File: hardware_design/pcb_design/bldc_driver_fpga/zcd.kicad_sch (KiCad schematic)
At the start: 8 parts, among them U1 LM339

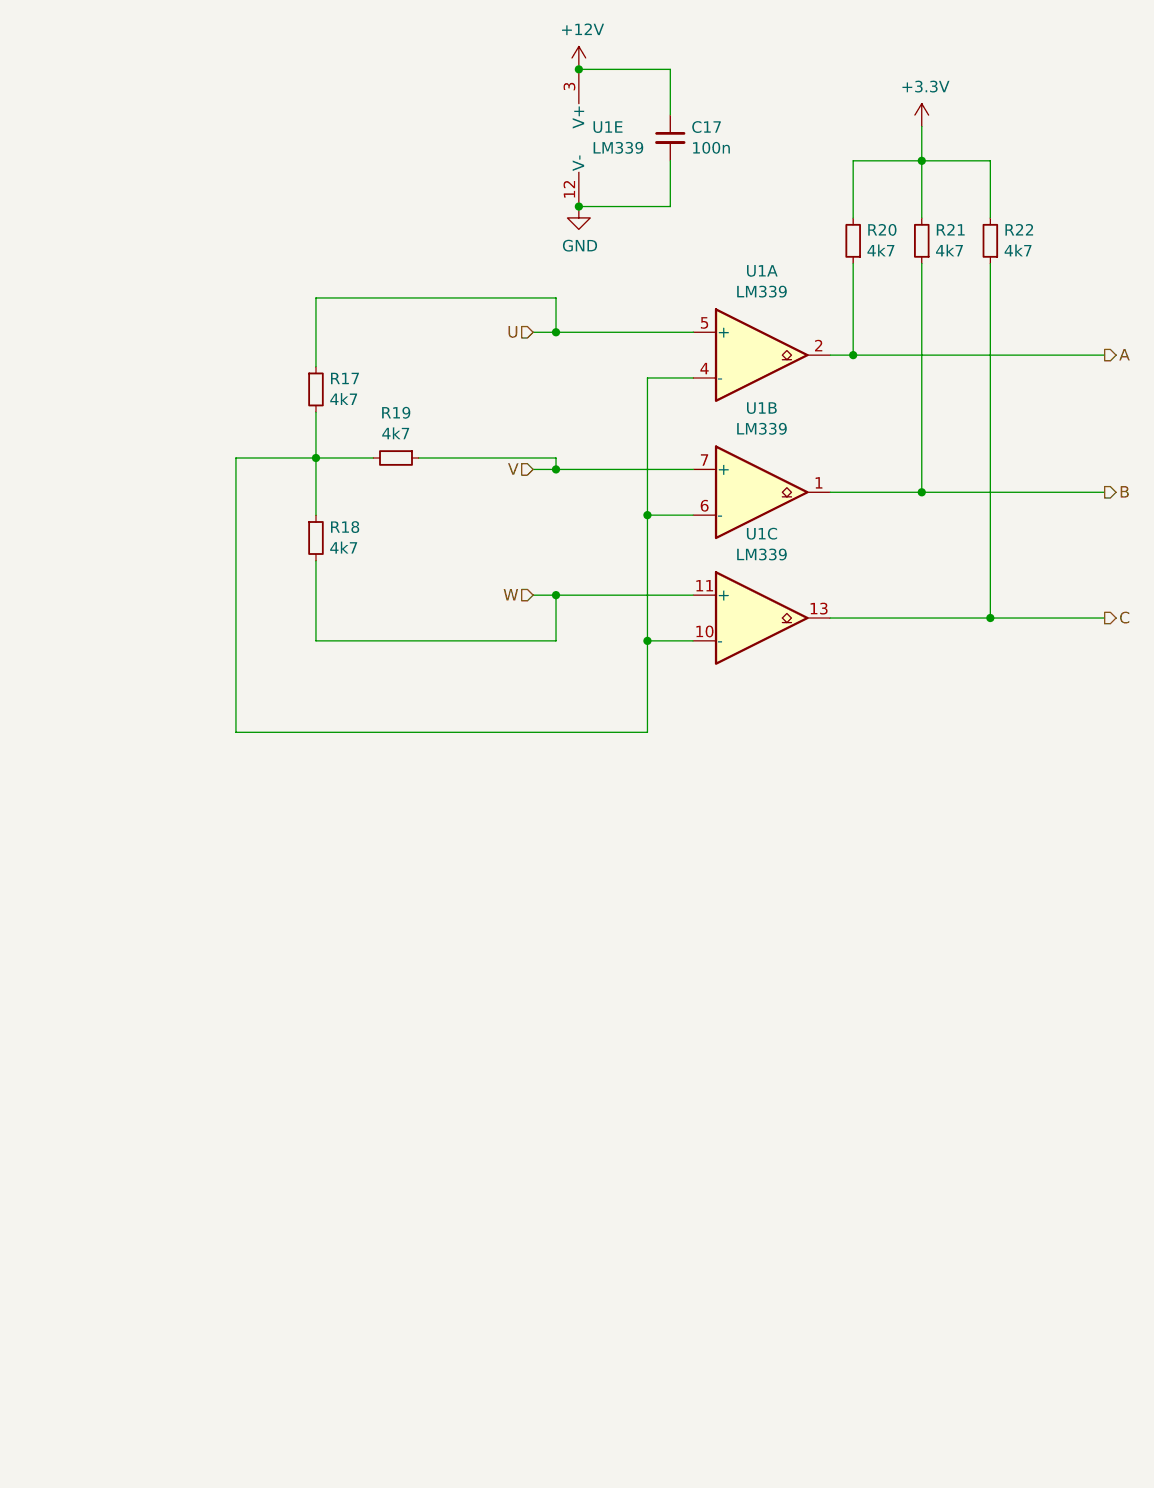
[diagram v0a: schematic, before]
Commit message: Implemented pure sinewave drive from programmable logic. Set up time base generator for ADC.
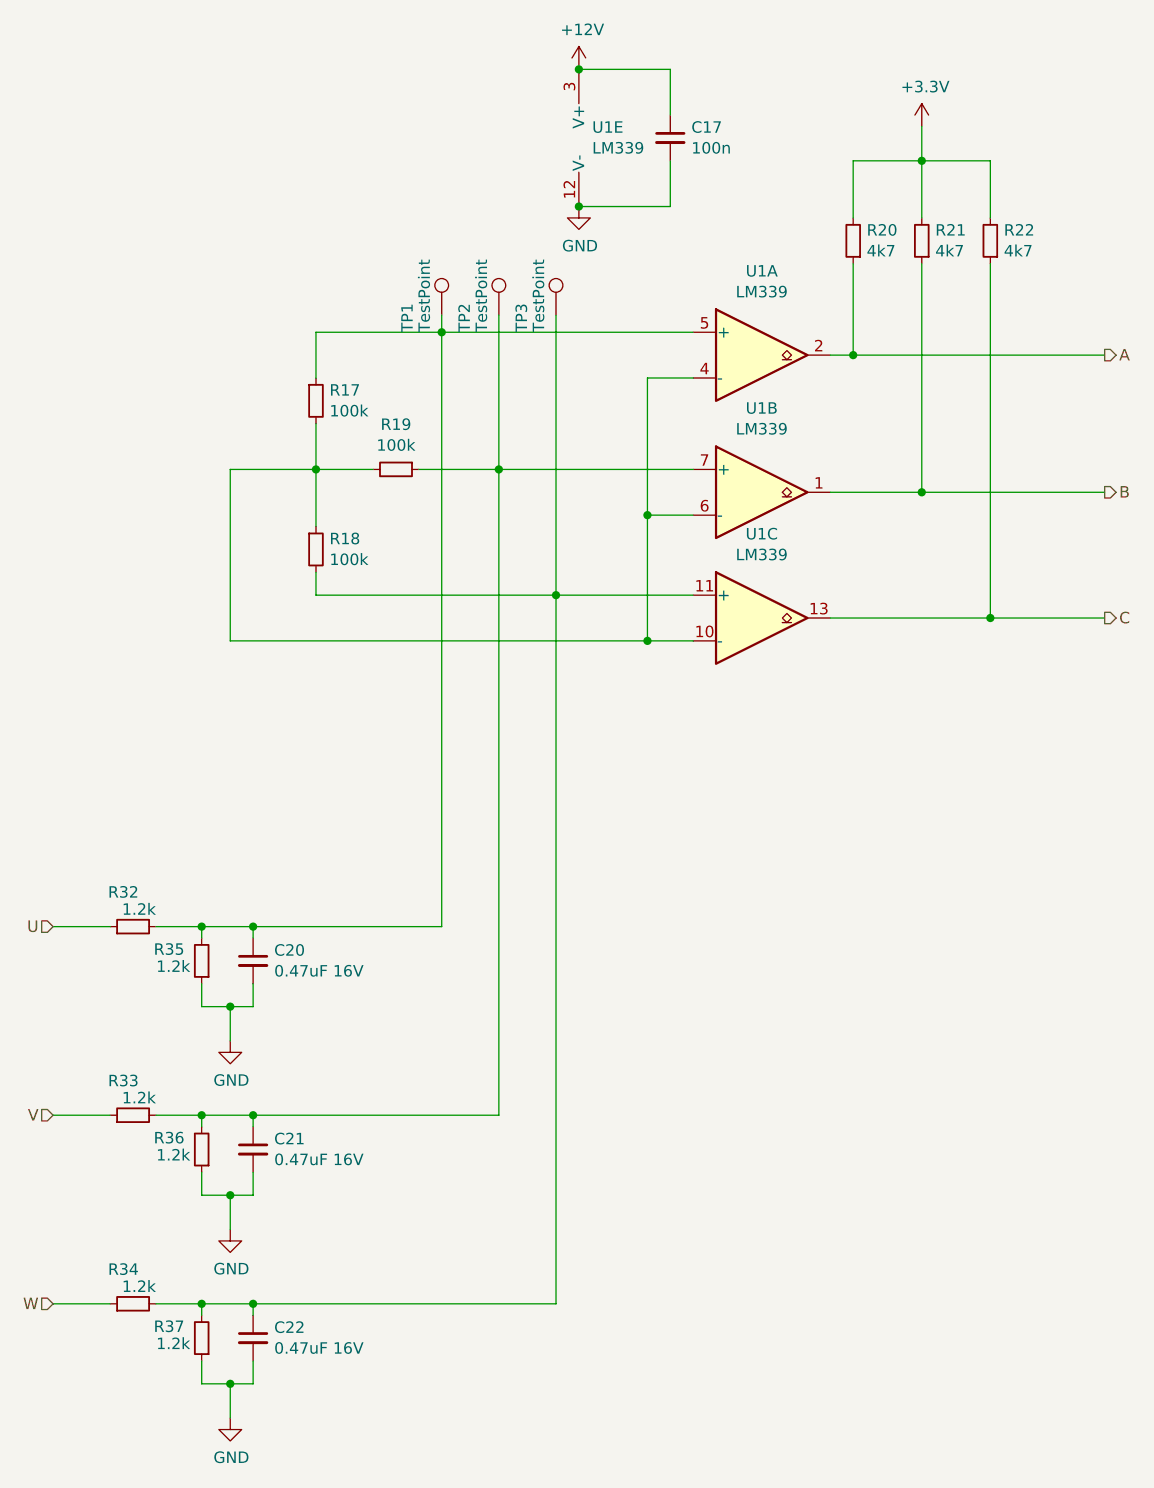
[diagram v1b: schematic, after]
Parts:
- added C20, C21, C22: 0.47uF 16V, Capacitor_SMD:C_0603_1608Metric_Pad1.08x0.95mm_HandSolder, symbol Device:C_Small
- added R32, R33, R34, R35, R36, R37: 1.2k, Resistor_SMD:R_0603_1608Metric_Pad0.98x0.95mm_HandSolder, symbol Device:R_Small
- added TP1, TP2, TP3: TestPoint, TestPoint:TestPoint_Pad_1.0x1.0mm, symbol Connector:TestPoint
- C17: footprint Capacitor_SMD:C_0805_2012Metric_Pad1.15x1.40mm_HandSolder -> Capacitor_SMD:C_0603_1608Metric_Pad1.08x0.95mm_HandSolder
- R17, R18, R19: value 4k7 -> 100k; footprint Resistor_SMD:R_0805_2012Metric_Pad1.15x1.40mm_HandSolder -> Resistor_SMD:R_0603_1608Metric_Pad0.98x0.95mm_HandSolder
- R20, R21, R22: footprint Resistor_SMD:R_0805_2012Metric_Pad1.15x1.40mm_HandSolder -> Resistor_SMD:R_0603_1608Metric_Pad0.98x0.95mm_HandSolder
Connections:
- net GND: now also C20.2, C21.2, C22.2, R35.1, R36.1, R37.1
- net U: now also R32.1; no longer R17.1, U1.5 (+)
- net V: now also R33.1; no longer R19.1, U1.7 (+)
- net W: now also R34.1; no longer R18.2, U1.11 (+)
- new net: C20.1, R17.1, R32.2, R35.2, TP1.1, U1.5 (+)
- new net: C21.1, R19.1, R33.2, R36.2, TP2.1, U1.7 (+)
- new net: C22.1, R18.2, R34.2, R37.2, TP3.1, U1.11 (+)
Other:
- moved on the sheet: R17, R18, R19
